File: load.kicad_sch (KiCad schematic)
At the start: 50 parts, among them IC3 TC4429CPA, IC4 TPS2121RUXR, J12 Conn_01x02_Socket, J13 Conn_01x02_Socket, J14 Conn_01x02_Socket, J16 Conn_01x02_Socket, J24 Conn_01x02_Socket, J3 Conn_01x02_Socket, J5 Conn_01x02_Socket, J9 Conn_01x03_Socket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

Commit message: Last update after PR4, mostly done I need revisions from rest of members with special attention on grounding layout
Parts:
- removed C27: 10n, Capacitor_SMD:C_1206_3216Metric_Pad1.33x1.80mm_HandSolder, symbol Device:C
- removed IC4: TPS2121RUXR, Package_DFN_QFN:Texas_VQFN-HR-12_2x2.5mm_P0.5mm, symbol PowerMUX:TPS2121RUXR
- removed R39: 51k, Resistor_SMD:R_0805_2012Metric_Pad1.20x1.40mm_HandSolder, symbol Device:R
- removed R40, R41: 4.7k, Resistor_SMD:R_1206_3216Metric_Pad1.30x1.75mm_HandSolder, symbol Device:R
- removed R42: 24k, Resistor_SMD:R_0805_2012Metric_Pad1.20x1.40mm_HandSolder, symbol Device:R
- removed R43: 100k, Resistor_SMD:R_1206_3216Metric_Pad1.30x1.75mm_HandSolder, symbol Device:R
- removed TP1, TP2: TestPoint, TestPoint:TestPoint_Pad_D1.0mm, symbol Connector:TestPoint
- added D6: LED, LED_SMD:LED_0805_2012Metric_Pad1.15x1.40mm_HandSolder, symbol Device:LED
- added R33: 1k, Resistor_SMD:R_1206_3216Metric_Pad1.30x1.75mm_HandSolder, symbol Device:R
- added SW4: SW_Push_DPDT, Latch_PB:SW_DPDT_XLX, symbol Switch:SW_Push_DPDT
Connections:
- net Highest_Power_Supply is gone; now on net +5V: C12.1, C15.1, C19.1, IC3.1 (VDD_1), IC3.8 (VDD_2)
- net POT_CS is gone; now on net GND: VR1.3 (A1)
- net POT_MISO is gone; now on net GND: VR1.5 (A0)
- net +3.3V: now also VR1.8 (SHDN), SW4.6 (C); no longer VR1.7 (SHDN)
- net GND: now also D6.1 (K), SW4.4 (A)
- net NOT_Converter_Duty: now reaches IC3.2 (INPUT), U3.4
- net POT_MOSI renamed POT_SDA
- net POT_SCK renamed POT_SCL
- new net: D6.2 (A), R33.2
- new net SELECT_CONVERTER: R33.1, SW4.5 (B)
- no-connect marks 1 -> 4
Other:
- note added: "Latch button so we can control whether the hand made or module converter will be used."
- note added: "Level Shifter Circuit"
- note added: "This gate driver has an inverted output, we could invert the PWM signal directly from the uC but I(Hiram) chose to use a spare inverter from the SN74HC14 instead, the drawback is that there is a tiny loss because propagation delays but I think it is a worth price for not dealing with inverted duty cycles in software"
- note removed: "PowerMUX"
- note removed: "TPS2121RUXR in Highest Voltage Configuration"
- note removed: "This gate driver has an inverted output, we could invert the PWM signal directly from the uC but I(Hiram) chose to use a spare inverter from the SN74HC14 instead"
- moved on the sheet: C15, U3B

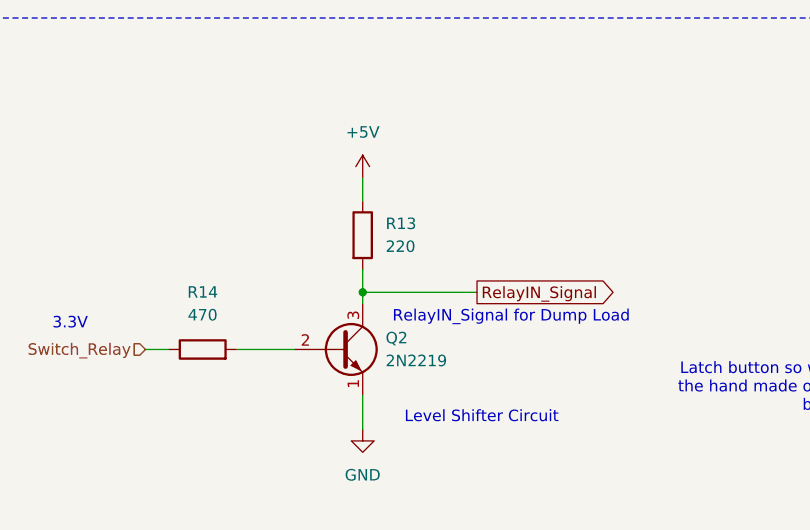
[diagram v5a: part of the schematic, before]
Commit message: added two more testpoints
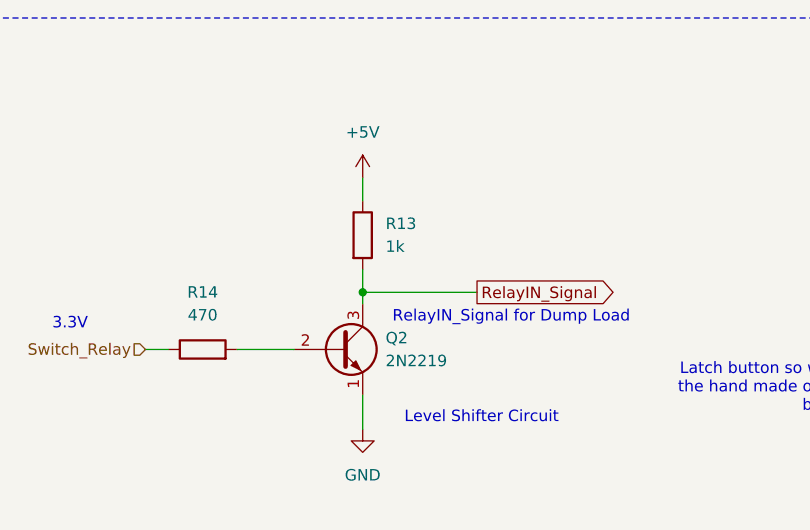
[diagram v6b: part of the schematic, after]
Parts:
- R13: value 220 -> 1k
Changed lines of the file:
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@@
 			)
 		)
-		(property "Value" "220"
+		(property "Value" "1k"
 			(at 59.69 35.5599 0)
 			(effects

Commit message: PCB finished, only final manufacturing files left, BOM, CPL
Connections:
- net GND: now also VR1.7 (NC)
- no-connect marks 4 -> 3
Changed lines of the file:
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@@
+	)
+	(junction
+		(at 58.42 99.06)
+		(diameter 0)
+		(color 0 0 0 0)
 	)
 	(junction
@@
 	)
 	(no_connect
-		(at 63.5 101.6)
-	)
-	(no_connect
 		(at 121.92 39.37)
 	)
@@
 	(wire
 		(pts
+			(xy 58.42 99.06) (xy 59.69 99.06)
+		)
+		(stroke
+			(width 0)
+			(type default)
+		)
+	)
+	(wire
+		(pts
 			(xy 207.01 34.29) (xy 207.01 39.37)
 		)
@@
 	(wire
 		(pts
+			(xy 58.42 101.6) (xy 58.42 99.06)
+		)
+		(stroke
+			(width 0)
+			(type default)
+		)
+	)
+	(wire
+		(pts
 			(xy 100.33 148.59) (xy 100.33 147.32)
 		)
@@
 	(wire
 		(pts
-			(xy 53.34 99.06) (xy 59.69 99.06)
+			(xy 53.34 99.06) (xy 58.42 99.06)
 		)
 		(stroke
@@
 		)
 		(stroke
+			(width 0)
+			(type default)
+		)
+	)
+	(wire
+		(pts
+			(xy 63.5 101.6) (xy 58.42 101.6)
+		)
+		(stroke
